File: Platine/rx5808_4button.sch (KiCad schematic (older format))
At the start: 54 parts, among them IC1 ATMEGA328-A, P1 CONN_01X02, P2 CONN_01X05, P5 BNC, P6 CONN_01X04, P7 CONN_02X05, U1 TPS62160, U2 RX5808, U3 sn74lvc1g3157, U4 MCPL3-BC-V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

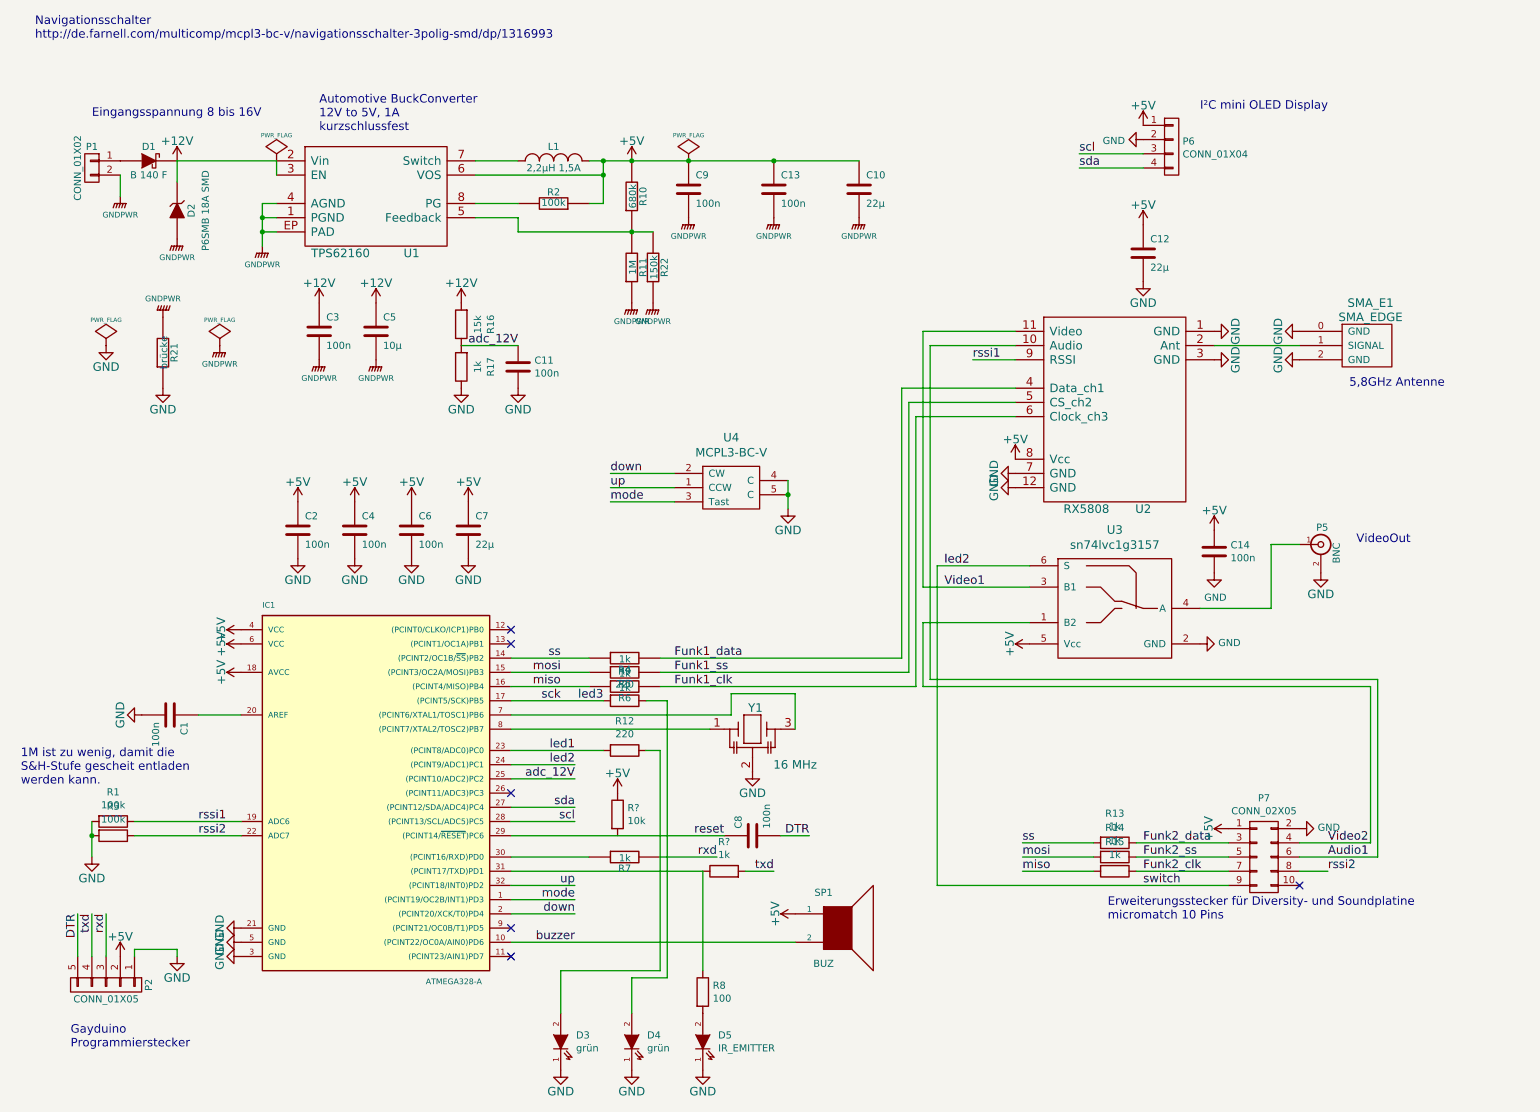
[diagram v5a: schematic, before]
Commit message: jetzt auch layout geändert. micromatchbuchse und/oder buzzer sollten noch verschoben werden!
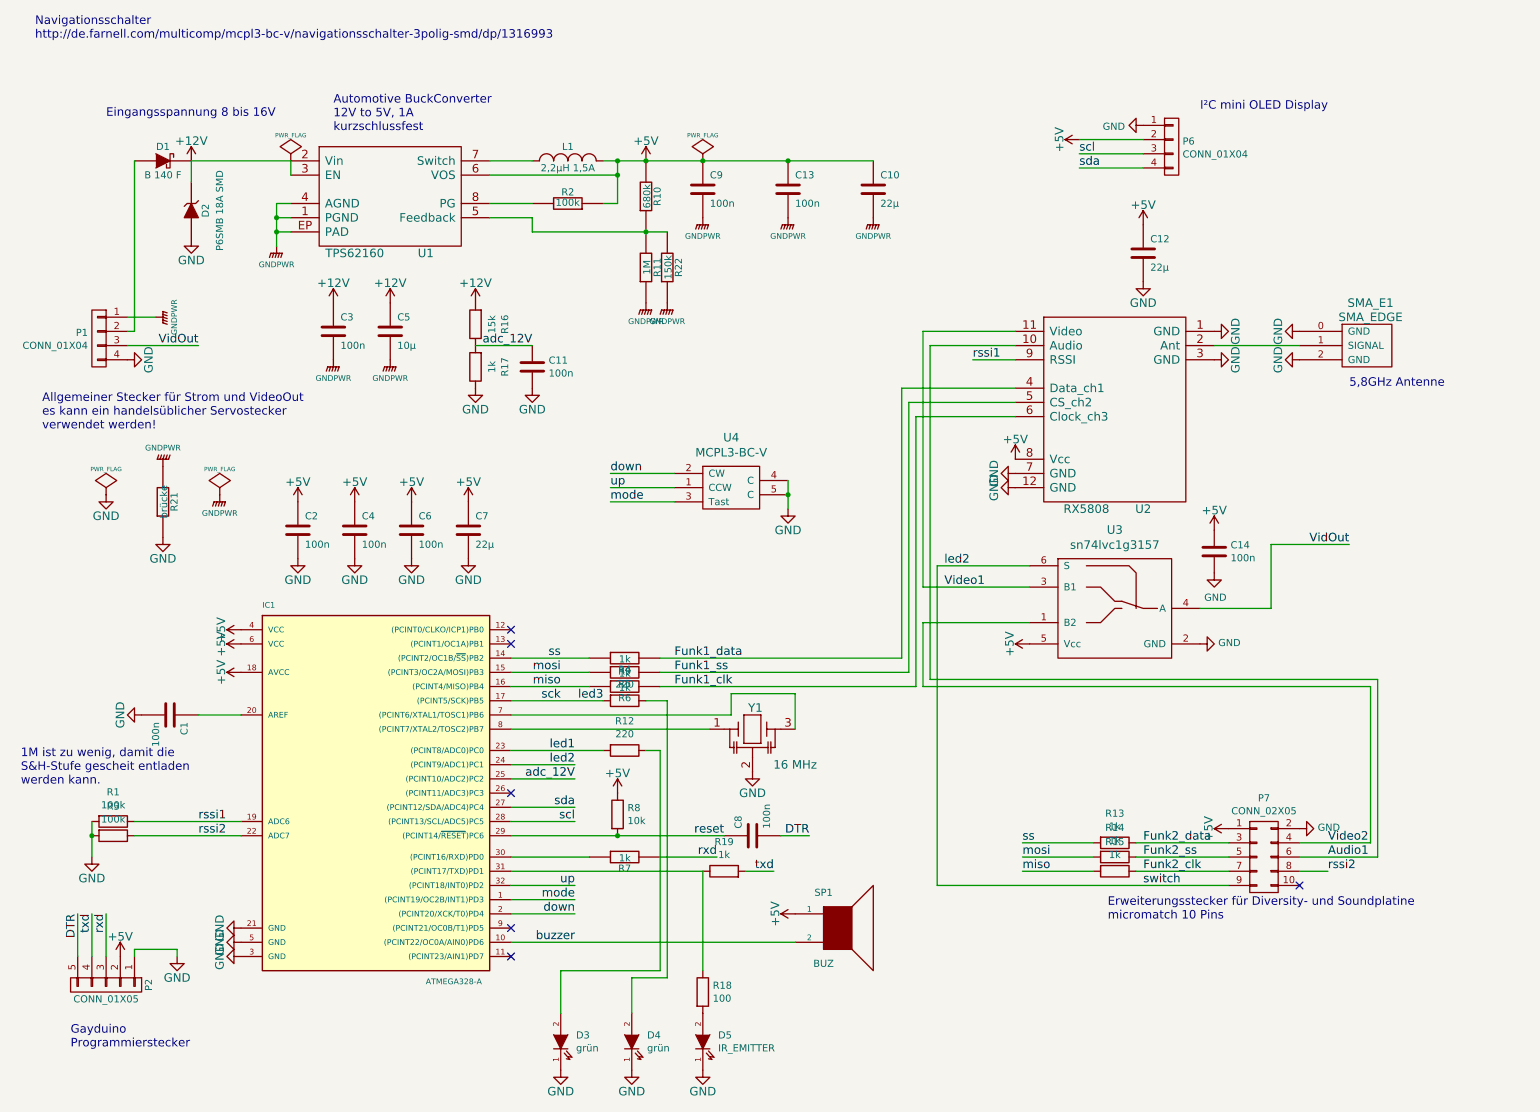
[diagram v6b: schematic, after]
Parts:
- removed P1: CONN_01X02, Sockets_MOLEX_KK-System:Socket_MOLEX-KK-RM2-54mm_Lock_2pin_straight, symbol CONN_01X02
- removed P5: BNC, Pin_Headers:Pin_Header_Angled_1x02, symbol BNC
- added P1: CONN_01X04, Connectors_JST:JST_XH_S04B-XH-A_04x2.50mm_Angled, symbol CONN_01X04
- R18, R19, R8: renamed from R?; footprint (none) -> Resistors_SMD:R_0603
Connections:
- net +5V: now also P6.2 (P2); no longer P6.1 (P1)
- net GND: now also D2.2 (A), P6.1 (P1), P1.4 (P4); no longer P6.2 (P2)
- net GNDPWR: now also P1.1 (P1); no longer D2.2 (A)
- net reset: now also R8.2
- net VidOut: now reaches U3.4 (A)
- net VidOut: now also P1.3 (P3)
- net at D1.1 (A): now also P1.2 (P2)
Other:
- note added: "Allgemeiner Stecker für Strom und VideoOut\nes kann ein handelsüblicher Servostecker\nverwendet werden!"
- note removed: "VideoOut"
- moved on the sheet: C10, C11, C13, C3, C5, C9, D1, D2, L1, R10, R11, R16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

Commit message: fuses-datei für den Atmega328PB dazugefügt, Bootloaderstecker auf JST PH geändert, Filterkondensator und Widerstand für OLED hinzugefügt
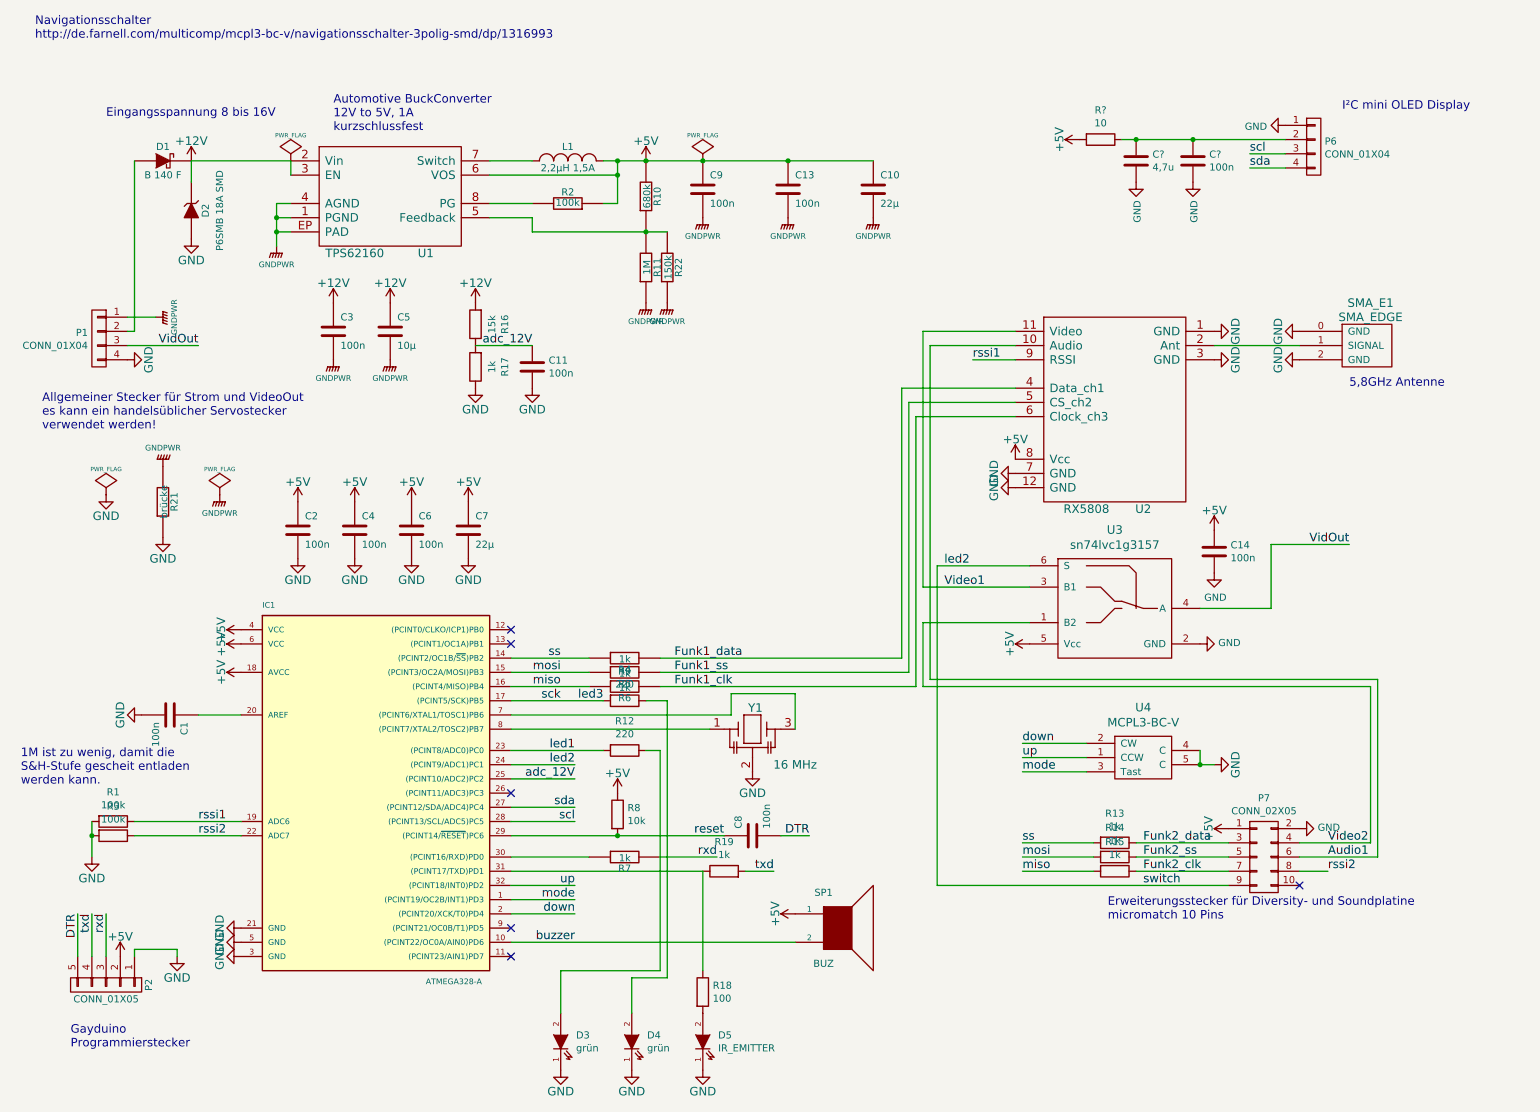
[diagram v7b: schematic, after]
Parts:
- removed C12: 22µ, Capacitors_SMD:C_1206, symbol C-RESCUE-rx5808_4button
- added C?: 100n, Capacitors_SMD:C_0603, symbol C
- added C?: 4,7u, Capacitors_SMD:C_0805, symbol C
- added R?: 10, Resistors_SMD:R_0805, symbol R
- P1: Herstellernummer (none) -> S4B-PH-K-S (LF)(SN)
- P2: footprint Pin_Headers:Pin_Header_Angled_1x05 -> Connectors_JST:JST_PH_S5B-PH-SM4-TB_05x2.00mm_Angled; Herstellernummer (none) -> S5B-PH-SM4-TB(LF)(SN)
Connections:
- net +5V: now also R?.2; no longer P6.2 (P2)
- net GND: now also C?.2, C?.2
- new net: C?.1, C?.1, P6.2 (P2), R?.1
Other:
- moved on the sheet: P6, U4

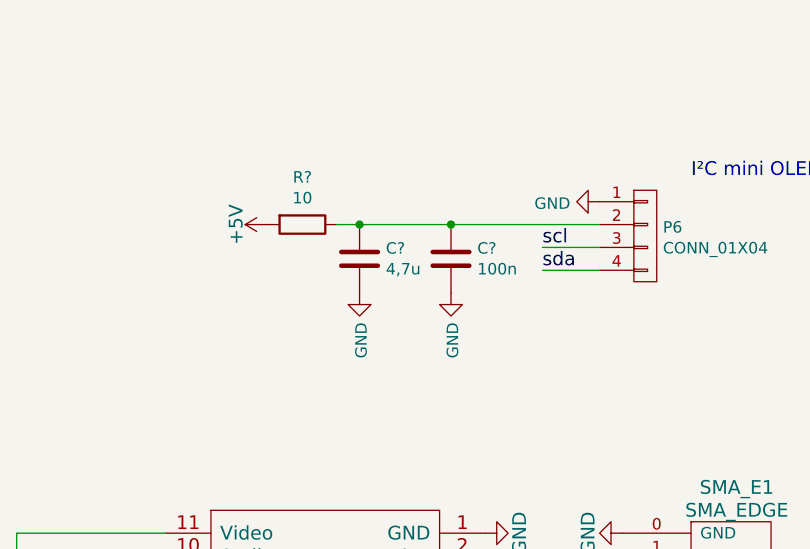
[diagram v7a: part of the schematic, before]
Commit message: RC-Filter für OLED hinzugefügt und eingelayoutet
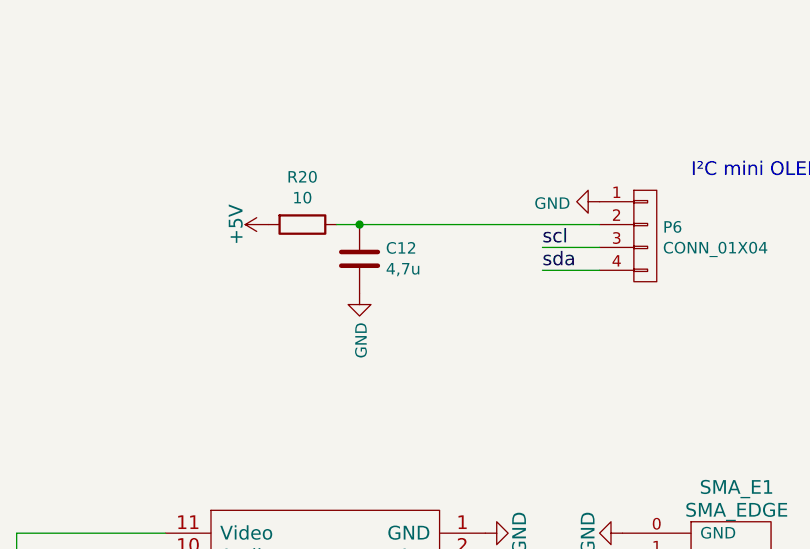
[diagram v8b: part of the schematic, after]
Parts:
- removed C?: 100n, Capacitors_SMD:C_0603, symbol C
- gave numbers to parts that had none: 2
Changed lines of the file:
@@
 Title "rx5808_3button_diversity"
 Date "Mi 25 Feb 2015"
-Rev "0.3"
+Rev "0.4"
 Comp ""
 Comment1 ""
@@
 $EndComp
 $Comp
-L C C?
-U 1 1 57568B0F
-P 8750 1100
-F 0 "C?" H 8865 1146 50  0000 L CNN
-F 1 "100n" H 8865 1055 50  0000 L CNN
-F 2 "Capacitors_SMD:C_0603" H 8788 950 50  0001 C CNN
-F 3 "" H 8750 1100 50  0000 C CNN
-	1    8750 1100
-	1    0    0    -1
-$EndComp
-$Comp
-L C C?
+L C C12
 U 1 1 57568ED3
 P 8350 1100
-F 0 "C?" H 8465 1146 50  0000 L CNN
+F 0 "C12" H 8465 1146 50  0000 L CNN
 F 1 "4,7u" H 8465 1055 50  0000 L CNN
 F 2 "Capacitors_SMD:C_0805" H 8388 950 50  0001 C CNN
@@
 $EndComp
 $Comp
-L GND #PWR?
-U 1 1 57569273
-P 8750 1250
-F 0 "#PWR?" H 8750 1000 50  0001 C CNN
-F 1 "GND" V 8758 1122 50  0000 R CNN
-F 2 "" H 8750 1250 50  0000 C CNN
-F 3 "" H 8750 1250 50  0000 C CNN
-	1    8750 1250
-	1    0    0    -1
-$EndComp
-$Comp
-L GND #PWR?
+L GND #PWR068
 U 1 1 575693C2
 P 8350 1250
-F 0 "#PWR?" H 8350 1000 50  0001 C CNN
+F 0 "#PWR068" H 8350 1000 50  0001 C CNN
 F 1 "GND" V 8358 1122 50  0000 R CNN
 F 2 "" H 8350 1250 50  0000 C CNN
@@
 Wire Wire Line
 	9150 1150 9400 1150
-Connection ~ 8750 950
-$Comp
-L R R?
+$Comp
+L R R20
 U 1 1 57569DCB
 P 8100 950
-F 0 "R?" V 7893 950 50  0000 C CNN
+F 0 "R20" V 7893 950 50  0000 C CNN
 F 1 "10" V 7984 950 50  0000 C CNN
 F 2 "Resistors_SMD:R_0805" V 7985 950 50  0001 C CNN
